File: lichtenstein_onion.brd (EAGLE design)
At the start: 73.9 x 54.2 mm, 49 parts, among them IC1 LM2852Y-3V3, J1 MAGJACK, U1 ONION-OMEGA2

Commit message: Fixed bulk capacitor footprints; made +V for output channels independent on output board
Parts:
- C13, C3, C5: value 100µF -> 47µF; device rcl:SMC_D -> rcl:CT7343
- C6: device rcl:SMC_D -> rcl:CT7343
- C9: value 100µF -> 47µF
- moved C3 2.84 mm to (46.0, 9.91), turned to 180 degrees
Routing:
- net V+: track 20.5 -> 22.1 mm
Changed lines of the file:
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@@
 <attribute name="SPICEPREFIX" value="C" x="34.036" y="9.652" size="1.778" layer="27" rot="R90" display="off"/>
 </element>
-<element name="C9" library="rcl" library_urn="urn:adsk.eagle:library:334" package="SMC_D" package3d_urn="urn:adsk.eagle:package:23434/1" value="100µF" x="19.558" y="23.114" smashed="yes" rot="MR180">
-<attribute name="MOUSER" value="581-NOSD107M006" x="19.558" y="23.114" size="1.778" layer="28" rot="MR180" display="off"/>
+<element name="C9" library="rcl" library_urn="urn:adsk.eagle:library:334" package="SMC_D" package3d_urn="urn:adsk.eagle:package:23434/1" value="47µF" x="19.558" y="23.114" smashed="yes" rot="MR180">
+<attribute name="MOUSER" value="581-TAJD476M016RNJV" x="19.558" y="23.114" size="1.778" layer="28" rot="MR180" display="off"/>
 <attribute name="NAME" x="16.002" y="20.447" size="0.8128" layer="26" font="vector" ratio="10" rot="MR180"/>
 <attribute name="SPICEPREFIX" value="C" x="19.558" y="23.114" size="1.778" layer="28" rot="MR180" display="off"/>
@@
 <attribute name="SPICEPREFIX" value="C" x="37.338" y="24.892" size="1.778" layer="27" display="off"/>
 </element>
-<element name="C13" library="rcl" library_urn="urn:adsk.eagle:library:334" package="SMC_D" package3d_urn="urn:adsk.eagle:package:23434/1" value="100µF" x="37.338" y="29.718" smashed="yes">
-<attribute name="MOUSER" value="581-NOSD107M006" x="37.338" y="29.718" size="1.778" layer="27" display="off"/>
+<element name="C13" library="rcl" library_urn="urn:adsk.eagle:library:334" package="CT7343" package3d_urn="urn:adsk.eagle:package:23304/2" value="47µF" x="37.338" y="29.718" smashed="yes">
+<attribute name="MOUSER" value="581-TAJD476M016RNJV" x="37.338" y="29.718" size="1.778" layer="27" display="off"/>
 <attribute name="NAME" x="33.782" y="32.385" size="0.8128" layer="25" font="vector" ratio="10"/>
 <attribute name="SPICEPREFIX" value="C" x="37.338" y="29.718" size="1.778" layer="27" display="off"/>
@@
 <attribute name="SPICEPREFIX" value="C" x="53.848" y="44.958" size="1.778" layer="27" display="off"/>
 </element>
-<element name="C3" library="rcl" library_urn="urn:adsk.eagle:library:334" package="SMC_D" package3d_urn="urn:adsk.eagle:package:23434/1" value="100µF" x="43.434" y="11.176" smashed="yes" rot="MR90">
-<attribute name="MOUSER" value="581-NOSD107M006" x="43.434" y="11.176" size="1.778" layer="28" rot="MR90" display="off"/>
-<attribute name="NAME" x="46.101" y="7.62" size="0.8128" layer="26" font="vector" ratio="10" rot="MR90"/>
-<attribute name="SPICEPREFIX" value="C" x="43.434" y="11.176" size="1.778" layer="28" rot="MR90" display="off"/>
+<element name="C3" library="rcl" library_urn="urn:adsk.eagle:library:334" package="CT7343" package3d_urn="urn:adsk.eagle:package:23304/2" value="47µF" x="45.974" y="9.906" smashed="yes" rot="MR180">
+<attribute name="MOUSER" value="581-TAJD476M016RNJV" x="45.974" y="9.906" size="1.778" layer="28" rot="MR180" display="off"/>
+<attribute name="NAME" x="42.418" y="7.239" size="0.8128" layer="26" font="vector" ratio="10" rot="MR180"/>
+<attribute name="SPICEPREFIX" value="C" x="45.974" y="9.906" size="1.778" layer="28" rot="MR180" display="off"/>
 </element>
 <element name="C4" library="rcl" library_urn="urn:adsk.eagle:library:334" package="C0805" package3d_urn="urn:adsk.eagle:package:23617/2" value="3.3nF" x="34.036" y="5.588" smashed="yes" rot="R90">
@@
 <attribute name="SPICEPREFIX" value="C" x="34.036" y="5.588" size="1.778" layer="27" rot="R90" display="off"/>
 </element>
-<element name="C5" library="rcl" library_urn="urn:adsk.eagle:library:334" package="SMC_D" package3d_urn="urn:adsk.eagle:package:23434/1" value="100µF" x="42.164" y="44.958" smashed="yes" rot="R180">
-<attribute name="MOUSER" value="581-NOSD107M006" x="42.164" y="44.958" size="1.778" layer="27" rot="R180" display="off"/>
+<element name="C5" library="rcl" library_urn="urn:adsk.eagle:library:334" package="CT7343" package3d_urn="urn:adsk.eagle:package:23304/2" value="47µF" x="42.164" y="44.958" smashed="yes" rot="R180">
+<attribute name="MOUSER" value="581-TAJD476M016RNJV" x="42.164" y="44.958" size="1.778" layer="27" rot="R180" display="off"/>
 <attribute name="NAME" x="45.72" y="42.291" size="0.8128" layer="25" font="vector" ratio="10" rot="R180"/>
 <attribute name="SPICEPREFIX" value="C" x="42.164" y="44.958" size="1.778" layer="27" rot="R180" display="off"/>
 </element>
-<element name="C6" library="rcl" library_urn="urn:adsk.eagle:library:334" package="SMC_D" package3d_urn="urn:adsk.eagle:package:23434/1" value="100µF" x="10.16" y="5.08" smashed="yes" rot="R270">
+<element name="C6" library="rcl" library_urn="urn:adsk.eagle:library:334" package="CT7343" package3d_urn="urn:adsk.eagle:package:23304/2" value="100µF" x="10.16" y="5.08" smashed="yes" rot="R270">
 <attribute name="MOUSER" value="581-NOSD107M006" x="10.16" y="5.08" size="1.778" layer="27" rot="R270" display="off"/>
 <attribute name="NAME" x="7.366" y="7.366" size="0.8128" layer="25" font="vector" ratio="10" rot="R90"/>
@@
 <wire x1="64.77" y1="43.18" x2="51.578" y2="43.18" width="0.1524" layer="16"/>
 <wire x1="51.578" y1="43.18" x2="49.738" y2="45.02" width="0.1524" layer="16"/>
-<wire x1="45.314" y1="44.958" x2="45.466" y2="44.958" width="0.1524" layer="1"/>
+<wire x1="45.364" y1="44.958" x2="45.466" y2="44.958" width="0.1524" layer="1"/>
 <wire x1="45.466" y1="44.958" x2="49.676" y2="44.958" width="0.1524" layer="1"/>
 <wire x1="49.676" y1="44.958" x2="49.73" y2="45.012" width="0.1524" layer="1"/>
@@
 <wire x1="52.832" y1="12.766" x2="55.118" y2="12.766" width="0.1524" layer="1"/>
 <wire x1="14.368" y1="6.604" x2="12.742" y2="8.23" width="0.4064" layer="1"/>
-<wire x1="12.742" y1="8.23" x2="10.16" y2="8.23" width="0.4064" layer="1"/>
-<wire x1="34.188" y1="29.718" x2="34.838" y2="29.718" width="0.254" layer="1"/>
+<wire x1="12.742" y1="8.23" x2="10.16" y2="8.28" width="0.4064" layer="1"/>
+<wire x1="34.138" y1="29.718" x2="34.838" y2="29.718" width="0.254" layer="1"/>
 <wire x1="34.838" y1="29.718" x2="36.388" y2="28.168" width="0.254" layer="1"/>
-<wire x1="34.188" y1="29.718" x2="34.188" y2="33.68" width="0.254" layer="1"/>
+<wire x1="34.138" y1="29.718" x2="34.188" y2="33.68" width="0.254" layer="1"/>
 <wire x1="34.188" y1="33.68" x2="45.466" y2="44.958" width="0.254" layer="1"/>
 <wire x1="16.408" y1="23.114" x2="16.459" y2="23.165" width="0.4064" layer="16"/>
@@
 <contactref element="C7" pad="1"/>
 <wire x1="5.522" y1="9.398" x2="8.992" y2="9.398" width="0.4064" layer="1"/>
-<wire x1="8.992" y1="9.398" x2="10.16" y2="8.23" width="0.4064" layer="1"/>
+<wire x1="8.992" y1="9.398" x2="10.16" y2="8.28" width="0.4064" layer="1"/>
 <contactref element="R1" pad="2"/>
 <contactref element="R2" pad="2"/>
@@
 <via x="19.558" y="23.114" extent="1-16" drill="0.35"/>
 <contactref element="C7" pad="2"/>
+<via x="50.8" y="12.192" extent="1-16" drill="0.35"/>
 </signal>
 <signal name="CONSOLE_RX">
@@
 <wire x1="34.036" y1="8.702" x2="37.15" y2="5.588" width="0.4064" layer="1"/>
 <wire x1="37.15" y1="5.588" x2="42.672" y2="5.588" width="0.4064" layer="1"/>
-<wire x1="43.434" y1="8.026" x2="43.434" y2="6.35" width="0.4064" layer="16"/>
-<wire x1="43.434" y1="6.35" x2="42.672" y2="5.588" width="0.4064" layer="16"/>
+<wire x1="42.774" y1="9.906" x2="42.672" y2="9.804" width="0.4064" layer="16"/>
+<wire x1="42.672" y1="9.804" x2="42.672" y2="5.588" width="0.4064" layer="16"/>
 </signal>
 <signal name="N$7">

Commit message: Cleaned up output board; added pull-ups to inputs on Lichtenstein board; moved some decoupling caps on FPGA output board
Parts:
- removed R14, R16, R17: 680R, rcl:M0805
- removed R15: 49.9R, rcl:M0805
- added RN1, RN2, RN3: 10k, resistor-net:CTS742C083
- R1, R4: value 10k -> 49.9R
- R11: value 680R -> 49.9R
- R2, R3: value 10k -> 4k7
- R6, R7: value 4k7 -> 680R
- R8, R9: value 49.9R -> 680R
- moved R4 63.8 mm to (67.8, 24.4)
- moved R8 58.6 mm to (9.40, 28.4), flipped to the top, turned to 90 degrees
- moved R11 56.8 mm to (63.5, 24.4), flipped to the bottom, turned to 270 degrees
- moved R1 54.2 mm to (65.8, 24.4)
- moved R6 50.7 mm to (4.32, 28.4), turned to 90 degrees
- moved R7 50.5 mm to (6.86, 28.4), turned to 90 degrees
- moved R9 49.7 mm to (11.9, 28.4), flipped to the top, turned to 90 degrees
- moved R3 48.5 mm to (55.1, 13.7), flipped to the top
- moved R12 44.3 mm to (52.8, 19.8)
- moved R13 44.0 mm to (55.1, 19.8)
- moved R2 43.7 mm to (52.8, 13.7), flipped to the top
- moved R10 16.6 mm to (10.9, 43.7), turned to 180 degrees
- moved R5 4.32 mm to (61.5, 24.4)
- moved C4 2.27 mm to (35.1, 3.56)
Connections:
- net +3V3: now also R10.1, RN1.5, RN1.6, RN1.7, RN1.8, RN2.5, RN2.6, RN2.7, RN2.8, RN3.5, RN3.6, RN3.7, RN3.8; no longer R1.2, R14.1, R4.2, R6.2, R7.2
- net ETH_LED_ACT: now also R12.2; no longer R16.2
- net ETH_LED_LINK: now also R13.2; no longer R17.2
- net ETH_RX+: now also R5.1; no longer R9.1
- net ETH_RX-: now also R11.1; no longer R15.1
- net ETH_TX+: now also R1.1; no longer R5.1
- net ETH_TX-: now also R4.1; no longer R8.1
- net I2C_SCL: now also R3.1; no longer R7.1
- net I2C_SDA: now also R2.1; no longer R6.1
- net INPUT0: now also RN2.1
- net INPUT1: now also RN2.2
- net INPUT2: now also RN2.3
- net INPUT3: now also RN2.4
- net INPUT4: now also RN3.4
- net INPUT5: now also RN3.3
- net INPUT6: now also RN3.2
- net INPUT7: now also RN3.1
- net N$1: now also R10.2; no longer R14.2
- net N$10: now also R8.2; no longer R12.2
- net N$11: now also R9.2; no longer R13.2
- net N$2: now also R6.2; no longer R10.2
- net N$3: now also R1.2, R4.2; no longer R5.2, R8.2
- net N$4: now also R12.1; no longer R16.1
- net N$5: now also R13.1; no longer R17.1
- net N$6: now also R11.2, R5.2; no longer R15.2, R9.2
- net N$9: now also R7.2; no longer R11.2
- net STATUS0: now also R6.1; no longer R10.1
- net STATUS1: now also R7.1; no longer R11.1
- net STATUS2: now also R8.1; no longer R12.1
- net STATUS3: now also R9.1; no longer R13.1
- net TEST0: now also RN1.4; no longer R1.1
- net TEST1: now also RN1.3; no longer R2.1
- net TEST2: now also RN1.2; no longer R3.1
- net TEST3: now also RN1.1; no longer R4.1
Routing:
- net +3V3: track 179.9 -> 209.2 mm, vias 2 -> 3
- net INPUT3: track 18.5 -> 34.1 mm
- net INPUT4: track 14.1 -> 27.1 mm
- net INPUT2: track 16.4 -> 29.1 mm
- net INPUT5: track 16.2 -> 26.8 mm
- net INPUT1: track 14.3 -> 23.9 mm
- net INPUT6: track 18.4 -> 26.5 mm
- net INPUT0: track 12.1 -> 18.3 mm
- net INPUT7: track 20.5 -> 25.2 mm
- net TEST3: track 40.0 -> 42.8 mm
- net N$8: track 2.19 -> 4.83 mm
- net TEST2: track 38.2 -> 39.4 mm
- net TEST0: track 32.7 -> 33.8 mm

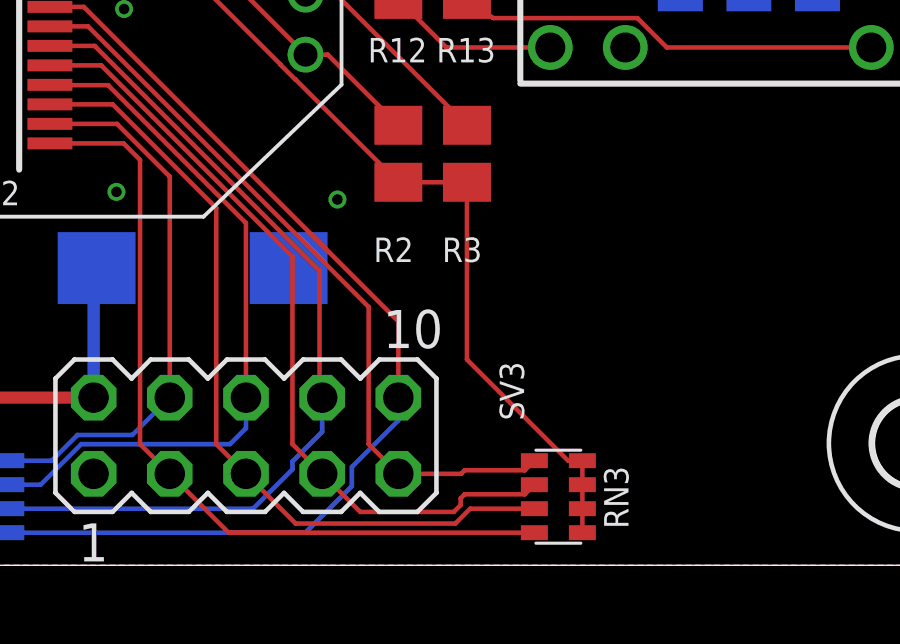
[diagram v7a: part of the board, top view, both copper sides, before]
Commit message: Moved resistor network inputs slightly
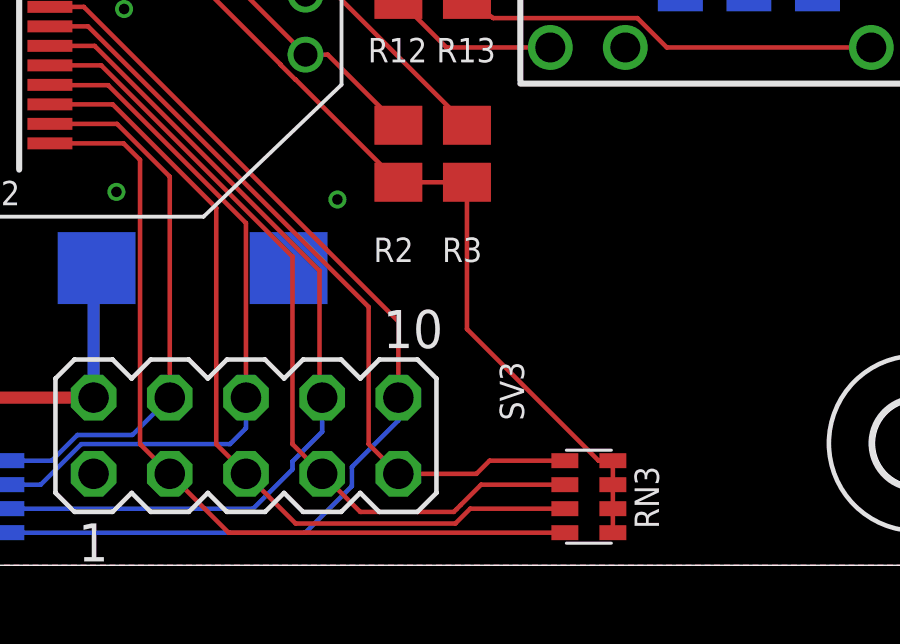
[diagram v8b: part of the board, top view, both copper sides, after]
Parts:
- moved RN3 1.02 mm to (59.2, 2.29)
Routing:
- net INPUT7: track 25.2 -> 26.2 mm
- net INPUT5: track 26.8 -> 27.8 mm
- net INPUT4: track 27.1 -> 28.1 mm
- net INPUT6: track 26.5 -> 27.4 mm
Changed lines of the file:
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@@
 <attribute name="OC_NEWARK" value="unknown" x="39.116" y="2.286" size="0.8128" layer="28" rot="MR270" display="off"/>
 </element>
-<element name="RN3" library="resistor-net" library_urn="urn:adsk.eagle:library:343" package="CTS742C083" package3d_urn="urn:adsk.eagle:package:24985/1" value="10k" x="58.166" y="2.286" smashed="yes" rot="R270">
-<attribute name="MF" value="" x="58.166" y="2.286" size="0.8128" layer="27" rot="R270" display="off"/>
-<attribute name="MOUSER" value="71-CRA04S0803103GRT7" x="58.166" y="2.286" size="0.8128" layer="27" rot="R270" display="off"/>
-<attribute name="MPN" value="" x="58.166" y="2.286" size="0.8128" layer="27" rot="R270" display="off"/>
-<attribute name="NAME" x="59.69" y="3.302" size="0.8128" layer="25" rot="R270"/>
-<attribute name="OC_FARNELL" value="unknown" x="58.166" y="2.286" size="0.8128" layer="27" rot="R270" display="off"/>
-<attribute name="OC_NEWARK" value="unknown" x="58.166" y="2.286" size="0.8128" layer="27" rot="R270" display="off"/>
+<element name="RN3" library="resistor-net" library_urn="urn:adsk.eagle:library:343" package="CTS742C083" package3d_urn="urn:adsk.eagle:package:24985/1" value="10k" x="59.182" y="2.286" smashed="yes" rot="R270">
+<attribute name="MF" value="" x="59.182" y="2.286" size="0.8128" layer="27" rot="R270" display="off"/>
+<attribute name="MOUSER" value="71-CRA04S0803103GRT7" x="59.182" y="2.286" size="0.8128" layer="27" rot="R270" display="off"/>
+<attribute name="MPN" value="" x="59.182" y="2.286" size="0.8128" layer="27" rot="R270" display="off"/>
+<attribute name="NAME" x="60.706" y="3.302" size="0.8128" layer="25" rot="R270"/>
+<attribute name="OC_FARNELL" value="unknown" x="59.182" y="2.286" size="0.8128" layer="27" rot="R270" display="off"/>
+<attribute name="OC_NEWARK" value="unknown" x="59.182" y="2.286" size="0.8128" layer="27" rot="R270" display="off"/>
 </element>
 <element name="RN1" library="resistor-net" library_urn="urn:adsk.eagle:library:343" package="CTS742C083" package3d_urn="urn:adsk.eagle:package:24985/1" value="10k" x="7.874" y="17.526" rot="MR180">
@@
 <contactref element="RN3" pad="7"/>
 <contactref element="RN3" pad="6"/>
-<wire x1="58.966" y1="1.086" x2="58.966" y2="1.886" width="0.1524" layer="1"/>
-<wire x1="58.966" y1="1.886" x2="58.966" y2="2.686" width="0.1524" layer="1"/>
-<wire x1="58.966" y1="2.686" x2="58.966" y2="3.486" width="0.1524" layer="1"/>
-<wire x1="55.118" y1="12.766" x2="55.118" y2="6.858" width="0.1524" layer="1"/>
-<wire x1="55.118" y1="6.858" x2="58.49" y2="3.486" width="0.1524" layer="1"/>
-<wire x1="58.49" y1="3.486" x2="58.966" y2="3.486" width="0.1524" layer="1"/>
+<wire x1="59.982" y1="1.086" x2="59.982" y2="1.886" width="0.1524" layer="1"/>
+<wire x1="59.982" y1="1.886" x2="59.982" y2="2.686" width="0.1524" layer="1"/>
+<wire x1="59.982" y1="2.686" x2="59.982" y2="3.486" width="0.1524" layer="1"/>
+<wire x1="55.118" y1="12.766" x2="55.118" y2="7.874" width="0.1524" layer="1"/>
+<wire x1="55.118" y1="7.874" x2="59.506" y2="3.486" width="0.1524" layer="1"/>
+<wire x1="59.506" y1="3.486" x2="59.982" y2="3.486" width="0.1524" layer="1"/>
 <wire x1="38.316" y1="1.086" x2="38.316" y2="1.886" width="0.1524" layer="16"/>
 <wire x1="38.316" y1="1.886" x2="38.316" y2="2.686" width="0.1524" layer="16"/>
@@
 <wire x1="45.212" y1="3.048" x2="44.2214" y2="4.0386" width="0.1524" layer="1"/>
 <contactref element="RN3" pad="4"/>
-<wire x1="57.366" y1="1.086" x2="47.174" y2="1.086" width="0.1524" layer="1"/>
+<wire x1="58.382" y1="1.086" x2="47.174" y2="1.086" width="0.1524" layer="1"/>
 <wire x1="47.174" y1="1.086" x2="45.212" y2="3.048" width="0.1524" layer="1"/>
 </signal>
@@
 <wire x1="46.7614" y1="11.9126" x2="46.7614" y2="4.0386" width="0.1524" layer="1"/>
 <contactref element="RN3" pad="3"/>
-<wire x1="57.366" y1="1.886" x2="55.226" y2="1.886" width="0.1524" layer="1"/>
+<wire x1="58.382" y1="1.886" x2="55.226" y2="1.886" width="0.1524" layer="1"/>
 <wire x1="55.226" y1="1.886" x2="54.7308" y2="1.3908" width="0.1524" layer="1"/>
 <wire x1="49.4092" y1="1.3908" x2="47.752" y2="3.048" width="0.1524" layer="1"/>
@@
 <wire x1="49.3014" y1="10.2884875" x2="49.3014" y2="4.0386" width="0.1524" layer="1"/>
 <contactref element="RN3" pad="2"/>
-<wire x1="57.366" y1="2.686" x2="57.0446" y2="2.3646" width="0.1524" layer="1"/>
-<wire x1="57.0446" y1="2.3646" x2="55.0433125" y2="2.3646" width="0.1524" layer="1"/>
-<wire x1="55.0433125" y1="2.3646" x2="54.9094" y2="2.2306875" width="0.1524" layer="1"/>
-<wire x1="54.9094" y1="2.2306875" x2="54.9094" y2="2.0074" width="0.1524" layer="1"/>
-<wire x1="54.9094" y1="2.0074" x2="54.68" y2="1.778" width="0.1524" layer="1"/>
+<wire x1="54.9094" y1="2.0074" x2="54.772" y2="1.87" width="0.1524" layer="1"/>
+<wire x1="54.772" y1="1.87" x2="54.68" y2="1.778" width="0.1524" layer="1"/>
 <wire x1="51.562" y1="1.778" x2="50.292" y2="3.048" width="0.1524" layer="1"/>
 <wire x1="54.68" y1="1.778" x2="51.562" y2="1.778" width="0.1524" layer="1"/>
+<wire x1="58.382" y1="2.686" x2="55.588" y2="2.686" width="0.1524" layer="1"/>
+<wire x1="55.588" y1="2.686" x2="54.9094" y2="2.0074" width="0.1524" layer="1"/>
 </signal>
 <signal name="INPUT7">
@@
 <wire x1="51.8414" y1="8.6106" x2="51.8414" y2="4.0386" width="0.1524" layer="1"/>
 <contactref element="RN3" pad="1"/>
-<wire x1="52.832" y1="3.048" x2="54.9267125" y2="3.048" width="0.1524" layer="1"/>
-<wire x1="54.9267125" y1="3.048" x2="55.0433125" y2="3.1646" width="0.1524" layer="1"/>
-<wire x1="55.0433125" y1="3.1646" x2="57.0446" y2="3.1646" width="0.1524" layer="1"/>
-<wire x1="57.0446" y1="3.1646" x2="57.366" y2="3.486" width="0.1524" layer="1"/>
+<wire x1="52.832" y1="3.048" x2="55.4347125" y2="3.048" width="0.1524" layer="1"/>
+<wire x1="58.382" y1="3.486" x2="55.8727125" y2="3.486" width="0.1524" layer="1"/>
+<wire x1="55.8727125" y1="3.486" x2="55.4347125" y2="3.048" width="0.1524" layer="1"/>
 </signal>
 <signal name="!OMEGA_RST">
